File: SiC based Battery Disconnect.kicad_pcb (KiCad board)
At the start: 4 copper layers, 111 x 74.6 mm, 93 parts, among them IC2 PIC16F15345T-E_SSVAO, IC4 MCP1792T-5002H_CB, IC5 MCP1792T-5002H_CB, J1 Input, J2 Output, J3 12V supply, J5 490107670612, J6 490107670612, Q1 IMW120R014M1H, Q2 IMW120R014M1H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

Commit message: updated the design
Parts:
- added H1: MountingHole, MountingHole:MountingHole_3.2mm_M3, F.Cu at (193.8, 137.3)
- added H2: MountingHole, MountingHole:MountingHole_3.2mm_M3, F.Cu at (115.0, 137.3)
- added H3: MountingHole, MountingHole:MountingHole_3.2mm_M3, F.Cu at (193.8, 100.9)
- added H4: MountingHole, MountingHole:MountingHole_3.2mm_M3, F.Cu at (115.0, 100.9)
- added RV1: Varistor, Varistor:VARRB750W100L2050T1200H2800, F.Cu at (150.3, 96.9)
- added TP1: 5001, 5001 tp:KEYSTONE_5001, F.Cu at (157.9, 125.1)
- added TP2: 5001, 5001 tp:KEYSTONE_5001, F.Cu at (157.9, 113.6)
- added TP3: TestPoint, TestPoint:TestPoint_Pad_D1.0mm, F.Cu at (147.9, 143.7)
- added TP5: 5001, 5001 tp:KEYSTONE_5001, F.Cu at (115.1, 146.1)
- added TP6: 5001, 5001 tp:KEYSTONE_5001, F.Cu at (136.6, 123.7)
- added TP7: 5001, 5001 tp:KEYSTONE_5001, F.Cu at (114.8, 122.8)
- added TP8: TestPoint, TestPoint:TestPoint_Pad_D1.0mm, F.Cu at (150.6, 134.3)
- added TP9: 5001, 5001 tp:KEYSTONE_5001, F.Cu at (146.4, 107.4)
- D7: value BZX84J-B22,115_22V -> BZX384-B22,115; footprint Package_TO_SOT_SMD:SOT-23 -> Diode_SMD:D_SOD-323
- Q6: value 2N7002bk,215 -> 2N7002BK,215
- TH100: moved to B.Cu
- moved C16 60.1 mm to (170.0, 70.3)
- moved C17 59.3 mm to (161.2, 70.3)
- moved R26 57.4 mm to (151.6, 70.3)
- moved R27 55.5 mm to (141.2, 70.3)
- moved TH100 53.7 mm to (126.8, 131.3), turned to 90 degrees
- moved R17 53.6 mm to (129.4, 93.4)
- moved R16 53.6 mm to (133.1, 93.5)
- moved R15 53.6 mm to (129.4, 93.4)
- moved R14 53.6 mm to (133.1, 93.5)
- moved C15 53.6 mm to (131.5, 90.0)
- moved R3 50.9 mm to (131.5, 82.6)
- moved J1 47.7 mm to (200.9, 84.7)
- moved J2 47.6 mm to (103.0, 84.0)
- moved Q1 47.6 mm to (164.0, 76.3)
- moved Q2 47.5 mm to (146.1, 87.2)
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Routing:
- net VSOURCE: track 22.4 -> 79.2 mm, vias 0 -> 1
- net DRIVER_EN2: track 0.00 -> 56.2 mm, vias 0 -> 2
- net DRIVER_EN1: track 0.00 -> 44.3 mm, vias 0 -> 2
- net Net-(Q1-D): track 29.8 -> 70.9 mm
- net Net-(Q1-G): track 0.00 -> 37.6 mm, vias 0 -> 1
- net VCC: track 0.00 -> 36.9 mm, vias 0 -> 2
- net Net-(U2A--): track 0.00 -> 34.8 mm, vias 0 -> 1
- net Net-(U2B--): track 0.00 -> 31.5 mm
- net Net-(U2B-+): track 0.00 -> 28.6 mm
- net RA3: track 0.00 -> 27.9 mm
- net Net-(U2A-+): track 0.00 -> 27.7 mm, vias 0 -> 1
- net Net-(Q3-G): track 0.00 -> 27.5 mm, vias 0 -> 2
- net VDDLV: track 0.00 -> 23.1 mm, vias 0 -> 3
- net BATT+(12V-48V): track 0.00 -> 22.9 mm
- net Net-(Q2-G): track 0.00 -> 22.5 mm
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- added copper zone on F.Cu, net Earth
- added copper zone on F.Cu, net GND
- added copper zone on F.Cu, net Net-(D7-K)
- added copper zone on F.Cu, net VCC
- added copper zone on B.Cu, net VDDHV
- added copper zone on B.Cu, net VDDLV
- added copper zone on F.Cu, net VSOURCE
- removed copper zone on In1.Cu, net Net-(J2-Pad1)
- removed copper zone on In2.Cu, net Net-(J2-Pad1)
- removed copper zone on In1.Cu, net Net-(Q1-D)
- removed copper zone on In2.Cu, net Net-(Q1-D)
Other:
- board size 111 x 74.6 mm -> 113 x 81 mm
- copper layers 4 -> 2

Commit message: design update
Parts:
- added C2: 4.7nF, Capacitor_SMD:C_1812_4532Metric, F.Cu at (174.7, 87.8)
- added D8: D, Diode_THT:D_DO-201AE_P12.70mm_Horizontal, F.Cu at (151.5, 65.3)
- added D9: D, Diode_THT:D_DO-201AE_P12.70mm_Horizontal, F.Cu at (166.9, 98.6)
- C16, R26, R27: moved to F.Cu
- C17: value 4.7nF -> 0.1uF; footprint Capacitor_SMD:C_1812_4532Metric -> Capacitor_SMD:C_0805_2012Metric; moved to F.Cu
- D5: value BZX84C4V3 -> BZX84C6V8
- moved C17 61.7 mm to (171.0, 131.2), turned to 0 degrees
- moved C16 29.9 mm to (140.6, 76.1), turned to 90 degrees
- moved R26 29.5 mm to (170.0, 93.3)
- moved R27 3.93 mm to (145.1, 70.2), turned to 0 degrees
- moved IC5 1.02 mm to (175.2, 128.3)
- moved TP8 0.43 mm to (150.3, 134.6)
- moved J1 0.40 mm to (200.9, 84.3)
- moved RV1 0.38 mm to (150.3, 97.3)
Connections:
- C16 pad 1: Net-(Q1-D) -> Net-(Q2-D)
- C16 pad 2: Net-(C16-Pad2) -> Net-(D8-A)
- C17 pad 1: Net-(C16-Pad2) -> Earth
- C17 pad 2: Net-(C17-Pad2) -> VDDLV
- R26 pad 1: Net-(C17-Pad2) -> Net-(D9-A)
- R26 pad 2: Net-(R26-Pad2) -> VSOURCE
- R27 pad 1: Net-(R26-Pad2) -> Net-(D8-A)
- R27 pad 2: Net-(J2-Pad1) -> VSOURCE
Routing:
- net Net-(J2-Pad1): track 34.2 -> 7.67 mm, vias 31 -> 17
- net VSOURCE: track 79.2 -> 105.2 mm
- net Net-(D9-A): track 0.00 -> 13.0 mm
- net Net-(D8-A): track 0.00 -> 10.8 mm
- net Net-(C16-Pad2): track 4.66 -> 0.00 mm
- net Net-(C17-Pad2): track 4.57 -> 0.00 mm
- net Net-(R26-Pad2): track 4.48 -> 0.00 mm
- net Net-(Q1-G): track 37.6 -> 41.5 mm
- net Net-(Q2-D): track 29.9 -> 33.1 mm
- net Net-(Q1-D): track 70.9 -> 69.5 mm, vias 32 -> 28
- net VDDLV: track 23.1 -> 24.5 mm
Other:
- board size 113 x 81 mm -> 113 x 86.7 mm

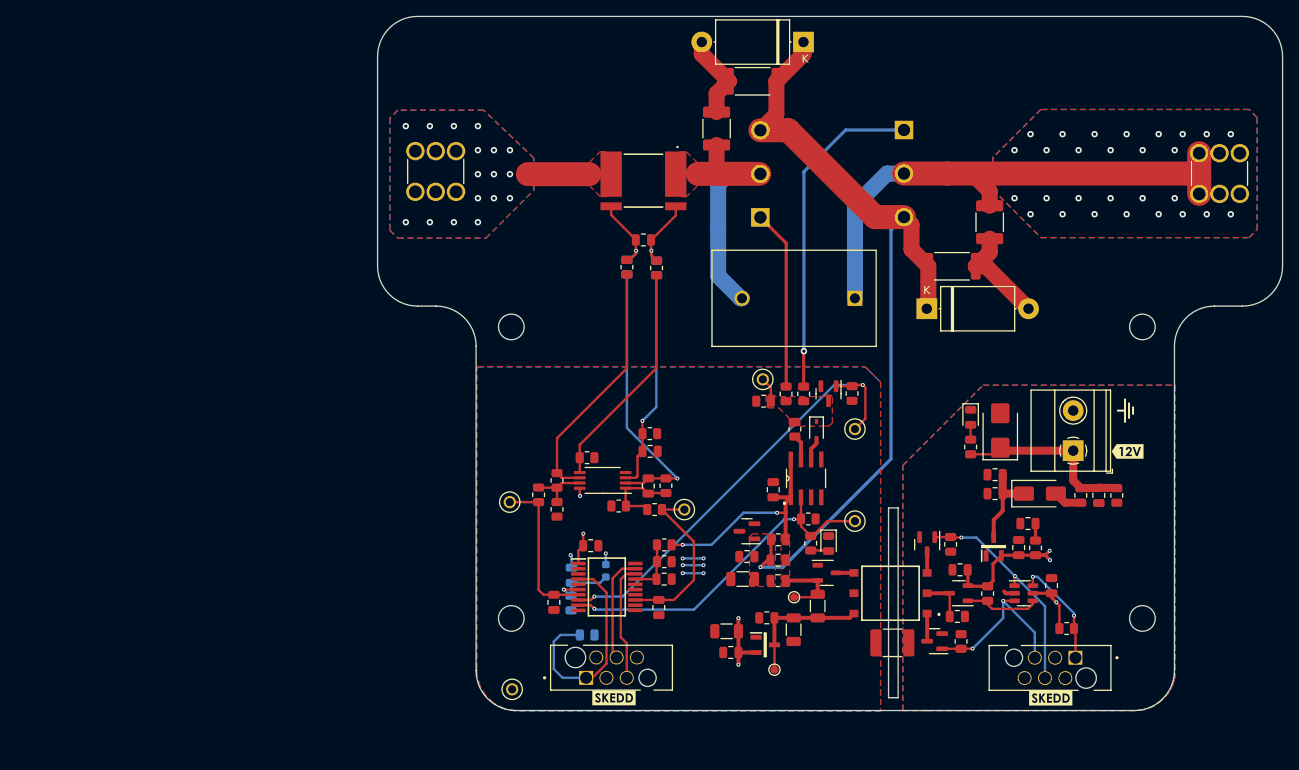
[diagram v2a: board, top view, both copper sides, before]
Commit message: Design with footprint error
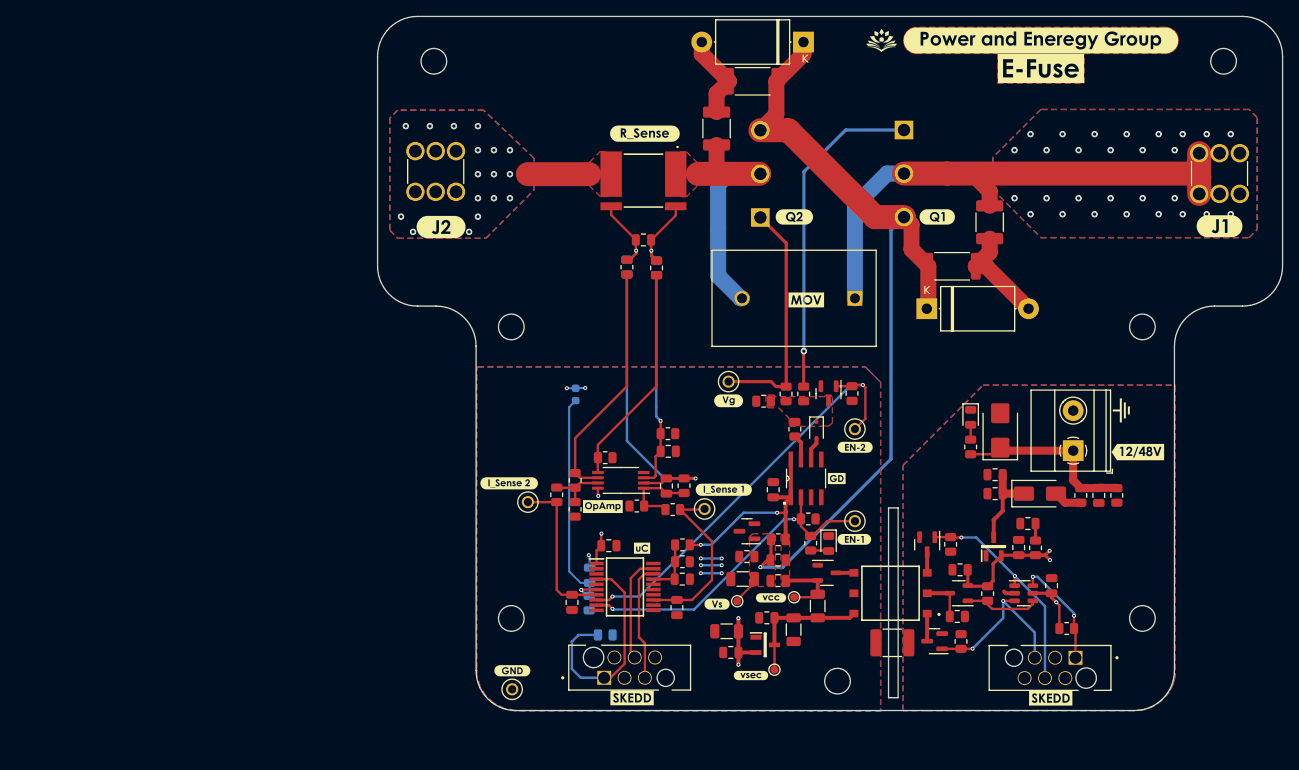
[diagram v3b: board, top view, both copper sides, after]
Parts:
- removed kibuzzard-64D0EA8A: G***, kibuzzard-64D0EA8A
- added G***: LOGO, Logo:iitdh, F.Cu at (161.2, 65.1)
- added H5: MountingHole, MountingHole:MountingHole_3.2mm_M3, F.Cu at (105.3, 67.7)
- added H6: MountingHole, MountingHole:MountingHole_3.2mm_M3, F.Cu at (203.9, 67.7)
- added H7: MountingHole, MountingHole:MountingHole_3.2mm_M3, F.Cu at (155.7, 145.1)
- added TP4: TestPoint, TestPoint:TestPoint_Pad_D1.0mm, F.Cu at (143.2, 135.1)
- added kibuzzard-650820C6: G***, kibuzzard-650820C6, F.Cu at (181.1, 65.1)
- added kibuzzard-65082383: G***, kibuzzard-65082383, F.Cu at (157.8, 127.4)
- added kibuzzard-6508239C: G***, kibuzzard-6508239C, F.Cu at (157.9, 115.9)
- added kibuzzard-6508248A: G***, kibuzzard-6508248A, F.Cu at (115.1, 143.8)
- added kibuzzard-65082582: G***, kibuzzard-65082582, F.Cu at (142.1, 110.1)
- added kibuzzard-650825C2: G***, kibuzzard-650825C2, F.Cu at (141.5, 121.2)
- added kibuzzard-650825F1: G***, kibuzzard-650825F1, F.Cu at (114.7, 120.4)
- added kibuzzard-65082C7F: G***, kibuzzard-65082C7F, B.Cu at (120.5, 111.5)
- added kibuzzard-65082D1D: G***, kibuzzard-65082D1D, F.Cu at (181.1, 68.6)
- added kibuzzard-65082D52: G***, kibuzzard-65082D52, F.Cu at (151.8, 97.5)
- added kibuzzard-65082DCF: G***, kibuzzard-65082DCF, B.Cu at (191.6, 128.8)
- added kibuzzard-65082FCA: G***, kibuzzard-65082FCA, F.Cu at (203.4, 88.3)
- added kibuzzard-65082FE1: G***, kibuzzard-65082FE1, F.Cu at (106.2, 88.4)
- added kibuzzard-6508304F: G***, kibuzzard-6508304F, F.Cu at (144.9, 144.4)
- added kibuzzard-6508305D: G***, kibuzzard-6508305D, F.Cu at (147.4, 134.7)
- added kibuzzard-650830BB: G***, kibuzzard-650830BB, F.Cu at (193.2, 116.5)
- added kibuzzard-650830F5: G***, kibuzzard-650830F5, F.Cu at (131.3, 128.5)
- added kibuzzard-65083125: G***, kibuzzard-65083125, F.Cu at (155.6, 119.8)
- added kibuzzard-6508313B: G***, kibuzzard-6508313B, F.Cu at (126.4, 123.3)
- added kibuzzard-650834CF: G***, kibuzzard-650834CF, F.Cu at (140.7, 135.5)
- added kibuzzard-6508355A: G***, kibuzzard-6508355A, F.Cu at (168.2, 87.1)
- added kibuzzard-6508356A: G***, kibuzzard-6508356A, F.Cu at (150.3, 87.1)
- added kibuzzard-650835E3: G***, kibuzzard-650835E3, F.Cu at (131.7, 76.7)
- moved TH100 22.3 mm to (123.0, 109.3)
- moved TP9 4.29 mm to (142.1, 107.7)
- moved TP6 2.52 mm to (139.1, 123.6)
- moved C11 2.26 mm to (134.6, 116.4)
- moved C12 2.26 mm to (122.6, 135.3)
- moved C13 2.26 mm to (135.7, 135.9)
- moved C6 2.26 mm to (127.2, 128.2)
- moved C9 2.26 mm to (136.4, 132.4)
- moved IC2 2.26 mm to (129.2, 133.3)
- moved R13 2.26 mm to (136.4, 128.1)
- moved R18 2.26 mm to (123.0, 120.0)
- moved R20 2.26 mm to (123.0, 123.7)
- moved R21 2.26 mm to (120.7, 121.8)
- moved R22 2.26 mm to (130.7, 123.2)
- moved R23 2.26 mm to (135.2, 123.7)
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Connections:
- TP9 pad TP: Net-(D7-K) -> Net-(Q2-G)
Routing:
- net Net-(IC2-RC4): track 9.27 -> 29.7 mm
- net Net-(Q2-G): track 22.5 -> 29.9 mm
- net VSOURCE: track 105.2 -> 108.9 mm
- net Net-(U2A--): track 34.8 -> 38.0 mm
- net Net-(D7-K): track 3.14 -> 0.00 mm
- net DRIVER_EN2: track 56.2 -> 53.9 mm
- net DRIVER_EN1: track 44.3 -> 42.1 mm
- net VCC: track 37.3 -> 35.0 mm
- net Net-(U2B-+): track 28.6 -> 27.7 mm
- net Net-(U2B--): track 31.5 -> 30.6 mm
- net GND: track 10.8 -> 11.7 mm, vias 8 -> 9
- added copper zone on F.Cu, net (none)

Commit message: Final Design
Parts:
- removed kibuzzard-650820C6: G***, kibuzzard-650820C6
- removed kibuzzard-65082DCF: G***, kibuzzard-65082DCF
- added C30: 0.1uF, Capacitor_SMD:C_0805_2012Metric, F.Cu at (124.2, 121.3)
- added kibuzzard-651F86C6: G***, kibuzzard-651F86C6, B.Cu at (191.6, 128.8)
- added kibuzzard-651F886F: G***, kibuzzard-651F886F, F.Cu at (181.1, 65.1)
- added kibuzzard-6557C38A: G***, kibuzzard-6557C38A, F.Cu at (181.1, 72.0)
- D3: value SM6T39A -> SM6T68CA
- IC2: value PIC16F15345T-E_SSVAO -> PIC16F15345-I/SO; footprint PIC16F15345T-E_SSVAO:SOP65P780X200-20N -> PIC16F15345-ISO:SOIC127P1030X265-20N
- J3: value 12V supply -> 12V/48V supply
- TP5: value 5001 -> 5001/TestPoint
- U2: footprint Package_SO:TSSOP-8_4.4x3mm_P0.65mm -> MCP6022-E_SN:SOIC127P599X175-8N
- moved kibuzzard-6508313B 14.5 mm to (131.5, 109.7)
- moved TH100 5.70 mm to (127.5, 112.8)
- moved C6 4.79 mm to (124.5, 124.2)
- moved R25 4.54 mm to (124.2, 113.4)
- moved R23 4.17 mm to (131.7, 121.3)
- moved C10 4.09 mm to (120.9, 130.6)
- moved R12 4.09 mm to (120.8, 134.1)
- moved kibuzzard-65082C7F 4.03 mm to (124.5, 111.0)
- moved kibuzzard-650830F5 4.00 mm to (131.3, 124.5)
- moved C14 3.98 mm to (131.1, 118.5)
- moved R24 3.91 mm to (133.3, 118.6)
- moved U2 3.75 mm to (126.0, 117.4)
- moved R22 3.52 mm to (127.7, 121.3)
- moved kibuzzard-650825C2 3.47 mm to (138.9, 118.9)
- moved TP7 3.25 mm to (114.9, 120.3)
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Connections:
- net Net-(Q3-G) renamed RA0_{lv}
- net Net-(Q5-G) renamed RA1_{lv}
- net Net-(U1-RA3) renamed RA3_{lv}
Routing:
- net I_SENSE_ANB4: track 21.9 -> 29.4 mm
- net Net-(U2A--): track 38.0 -> 33.5 mm
- net RA0: track 13.4 -> 16.6 mm
- net Net-(D9-A): track 13.0 -> 16.0 mm
- net VSOURCE: track 108.9 -> 111.7 mm
- net RA1: track 14.7 -> 17.3 mm
- net Net-(U2B-+): track 27.7 -> 25.2 mm
- net Net-(IC2-RC4): track 29.7 -> 27.3 mm
- net Net-(U2A-+): track 27.2 -> 24.9 mm
- net DRIVER_EN2: track 53.9 -> 56.2 mm
- net Net-(D8-A): track 10.8 -> 13.0 mm
- net Net-(U2B--): track 30.6 -> 28.4 mm
- net DRIVER_EN1: track 42.1 -> 44.1 mm
- net Net-(C14-Pad2): track 10.4 -> 8.84 mm
- net RA3: track 27.9 -> 29.4 mm
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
